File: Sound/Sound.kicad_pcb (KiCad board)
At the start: 4 copper layers, 133.6 x 74.7 mm, 35 parts, among them J1 Expansion_Connector, U1 74HCT74, U2 74HCT08, U3 74HCT21, U4 74HCT04, U5 LM386, U6 LM386, U7 LM386

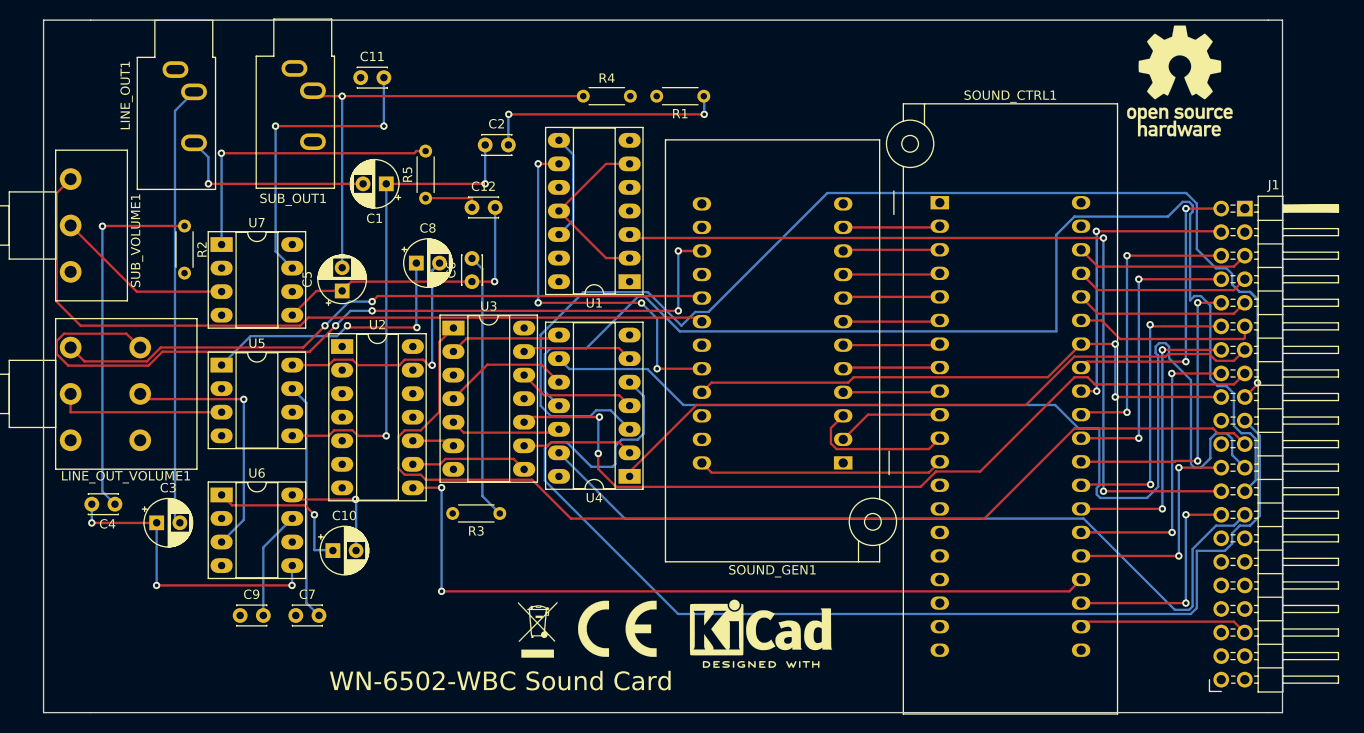
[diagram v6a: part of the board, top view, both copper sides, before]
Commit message: Fat trimming...
Trimmed out some old files and edited the docs.
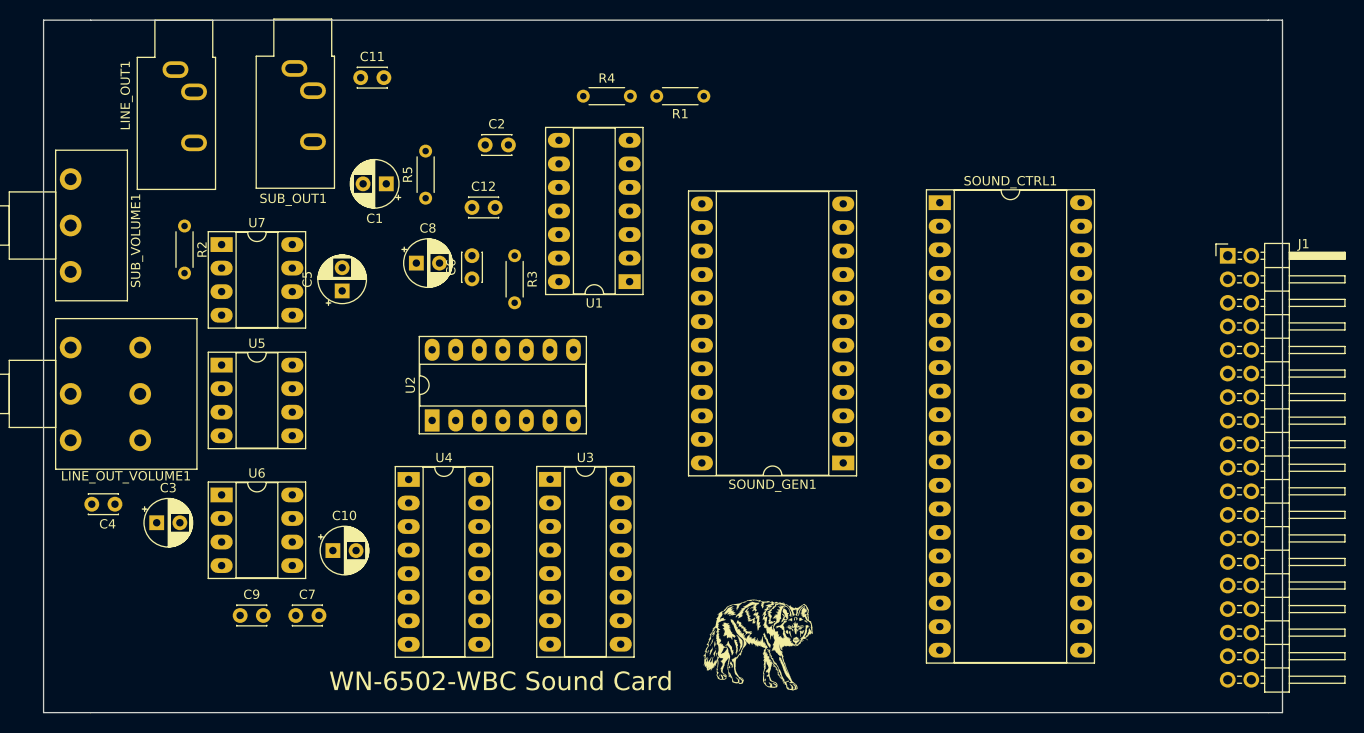
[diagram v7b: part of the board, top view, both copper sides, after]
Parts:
- removed REF**: OSHW-Logo_11.4x12mm_SilkScreen, Symbol:OSHW-Logo_11.4x12mm_SilkScreen
- removed REF**: WEEE-Logo_4.2x6mm_SilkScreen, Symbol:WEEE-Logo_4.2x6mm_SilkScreen
- removed REF**: CE-Logo_8.5x6mm_SilkScreen, Symbol:CE-Logo_8.5x6mm_SilkScreen
- removed REF**: KiCad-Logo2_6mm_SilkScreen, Symbol:KiCad-Logo2_6mm_SilkScreen
- added G***: LOGO, WolfNet:WolfNet-Logo_silkscreen, F.Cu at (128.3, 118.1)
- LINE_OUT1: value LINE OUT -> 3.5mm stereo
- SOUND_CTRL1: footprint Socket:DIP_Socket-40_W11.9_W12.7_W15.24_W17.78_W18.5_3M_240-1280-00-0602J -> Package_DIP:DIP-40_W15.24mm_Socket_LongPads
- SOUND_GEN1: footprint Socket:DIP_Socket-24_W11.9_W12.7_W15.24_W17.78_W18.5_3M_224-1275-00-0602J -> Package_DIP:DIP-24_W15.24mm_Socket_LongPads
- SUB_OUT1: value SUB OUT -> 3.5mm mono
- U2: value 74HCT08 -> 74HCT02
- U3: value 74HCT21 -> 74HCT138; footprint Package_DIP:DIP-14_W7.62mm_Socket_LongPads -> Package_DIP:DIP-16_W7.62mm_Socket_LongPads
- U4: value 74HCT04 -> 74HCT138; footprint Package_DIP:DIP-14_W7.62mm_Socket_LongPads -> Package_DIP:DIP-16_W7.62mm_Socket_LongPads
- moved R3 27.8 mm to (101.6, 76.2), turned to -90 degrees
- moved U4 23.8 mm to (90.2, 100.3), turned to 0 degrees
- moved U3 19.4 mm to (105.4, 100.3)
- moved U2 12.6 mm to (92.7, 94.0), turned to 90 degrees
- moved J1 7.14 mm to (178.5, 76.2)
- moved C6 0.30 mm to (97.0, 78.7)
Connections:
- net R\~W renamed R\~{W}
- net ~CS_SND renamed ~{CS_SND}
- net ~RESET renamed ~{RESET}
- J1 pad 20: (no net) -> unconnected-(J1-Pad20)
- J1 pad 22: (no net) -> unconnected-(J1-Pad22)
- J1 pad 28: ~CS_DEV -> CS_DEV
- J1 pad 29: (no net) -> unconnected-(J1-Pad29)
- J1 pad 30: (no net) -> unconnected-(J1-Pad30)
- J1 pad 31: (no net) -> unconnected-(J1-Pad31)
- J1 pad 32: (no net) -> unconnected-(J1-Pad32)
- J1 pad 33: (no net) -> unconnected-(J1-Pad33)
- J1 pad 34: (no net) -> unconnected-(J1-Pad34)
- J1 pad 35: (no net) -> unconnected-(J1-Pad35)
- J1 pad 36: (no net) -> unconnected-(J1-Pad36)
- J1 pad 38: (no net) -> unconnected-(J1-Pad38)
- SOUND_CTRL1 pad 13: (no net) -> unconnected-(SOUND_CTRL1-Pad13)
- SOUND_CTRL1 pad 14: (no net) -> unconnected-(SOUND_CTRL1-Pad14)
- SOUND_CTRL1 pad 15: (no net) -> unconnected-(SOUND_CTRL1-Pad15)
- SOUND_CTRL1 pad 16: (no net) -> unconnected-(SOUND_CTRL1-Pad16)
- SOUND_CTRL1 pad 17: (no net) -> unconnected-(SOUND_CTRL1-Pad17)
- SOUND_CTRL1 pad 18: (no net) -> unconnected-(SOUND_CTRL1-Pad18)
- SOUND_CTRL1 pad 19: (no net) -> unconnected-(SOUND_CTRL1-Pad19)
- SOUND_CTRL1 pad 21: (no net) -> unconnected-(SOUND_CTRL1-Pad21)
- SOUND_CTRL1 pad 23: ~CS_DEV -> Net-(SOUND_CTRL1-Pad23)
- SOUND_CTRL1 pad 24: Net-(SOUND_CTRL1-Pad24) -> CS_DEV
- SOUND_CTRL1 pad 39: (no net) -> unconnected-(SOUND_CTRL1-Pad39)
- SOUND_CTRL1 pad 40: (no net) -> unconnected-(SOUND_CTRL1-Pad40)
- SOUND_GEN1 pad 12: (no net) -> unconnected-(SOUND_GEN1-Pad12)
- SOUND_GEN1 pad 14: (no net) -> unconnected-(SOUND_GEN1-Pad14)
- SOUND_GEN1 pad 16: (no net) -> unconnected-(SOUND_GEN1-Pad16)
- U1 pad 5: (no net) -> unconnected-(U1-Pad5)
- U2 pad 1: (no net) -> Net-(SOUND_CTRL1-Pad23)
- U2 pad 10: Net-(U2-Pad10) -> (no net)
- U2 pad 2: (no net) -> Net-(U2-Pad2)
- U2 pad 3: (no net) -> Net-(U2-Pad3)
- U2 pad 8: Net-(SOUND_CTRL1-Pad24) -> (no net)
- U2 pad 9: Net-(U2-Pad9) -> (no net)
- U3 pad 1: A8 -> A4
- U3 pad 10: A5 -> unconnected-(U3-Pad10)
- U3 pad 11: (no net) -> unconnected-(U3-Pad11)
- U3 pad 12: Net-(U3-Pad12) -> unconnected-(U3-Pad12)
- U3 pad 13: Net-(U3-Pad13) -> unconnected-(U3-Pad13)
- U3 pad 14: VCC -> unconnected-(U3-Pad14)
- U3 pad 2: Net-(U3-Pad2) -> A6
- U3 pad 3: (no net) -> A7
- U3 pad 4: Net-(U3-Pad4) -> GND
- U3 pad 5: Net-(U3-Pad5) -> GND
- U3 pad 6: Net-(U2-Pad10) -> A5
- U3 pad 7: GND -> unconnected-(U3-Pad7)
- U3 pad 8: Net-(U2-Pad9) -> GND
- U3 pad 9: Net-(U3-Pad9) -> unconnected-(U3-Pad9)
- U4 pad 1: A4 -> A9
- U4 pad 10: Net-(U3-Pad4) -> unconnected-(U4-Pad10)
- U4 pad 11: A10 -> unconnected-(U4-Pad11)
- U4 pad 12: Net-(U3-Pad5) -> unconnected-(U4-Pad12)
- U4 pad 13: A11 -> unconnected-(U4-Pad13)
- U4 pad 14: VCC -> unconnected-(U4-Pad14)
- U4 pad 2: Net-(U3-Pad9) -> A10
- U4 pad 3: A6 -> A11
- U4 pad 4: Net-(U3-Pad12) -> GND
- U4 pad 5: A7 -> GND
- U4 pad 6: Net-(U3-Pad13) -> A8
- U4 pad 7: GND -> unconnected-(U4-Pad7)
- U4 pad 8: Net-(U3-Pad2) -> GND
- U4 pad 9: A9 -> unconnected-(U4-Pad9)
- U7 pad 8: (no net) -> unconnected-(U7-Pad8)
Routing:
- net GND: track 350.9 -> 0.00 mm
- net VCC: track 238.5 -> 0.00 mm
- net A10: track 129.0 -> 0.00 mm
- net A7: track 127.0 -> 0.00 mm
- net A6: track 126.0 -> 0.00 mm, vias 1 -> 0
- net A9: track 117.8 -> 0.00 mm
- net A8: track 116.8 -> 0.00 mm
- net 8MHz: track 91.3 -> 0.00 mm, vias 2 -> 0
- net Net-(LINE_OUT_VOLUME1-Pad4): track 90.3 -> 0.00 mm, vias 4 -> 0
- net A5: track 90.2 -> 0.00 mm, vias 2 -> 0
- net A11: track 88.8 -> 0.00 mm
- net Net-(SOUND_GEN1-Pad18): track 85.0 -> 0.00 mm
- net Net-(SOUND_CTRL1-Pad24): track 83.8 -> 0.00 mm, vias 2 -> 0
- net A4: track 72.9 -> 0.00 mm
- net Net-(LINE_OUT_VOLUME1-Pad1): track 71.7 -> 0.00 mm, vias 2 -> 0
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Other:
- net class Default removed

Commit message: 406 traces left to route...
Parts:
- moved G*** 48.3 mm to (176.5, 118.1)
- moved U2 39.5 mm to (125.7, 115.6), turned to 180 degrees
- moved J1 21.6 mm to (177.2, 54.6)
- moved SOUND_GEN1 16.1 mm to (138.4, 82.6)
- moved SOUND_CTRL1 15.9 mm to (147.4, 54.6)
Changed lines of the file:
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@@
   )
   (footprint "PC:Expansion_Connector_Board" (layer "F.Cu")
-    (at 178.5 76.21)
+    (at 177.23 54.62)
     (descr "Through hole angled pin header, 2x19, 2.54mm pitch, 6mm pin length, double rows")
     (tags "Through hole angled pin header THT 2x19 2.54mm double row")
@@
   )
   (footprint "Package_DIP:DIP-24_W15.24mm_Socket_LongPads" (layer "F.Cu")
-    (at 137.033 98.552 180)
+    (at 138.435 82.555 180)
     (descr "24-lead though-hole mounted DIP package, row spacing 15.24 mm (600 mils), Socket, LongPads")
     (tags "THT DIP DIL PDIP 2.54mm 15.24mm 600mil Socket LongPads")
@@
   )
   (footprint "Package_DIP:DIP-40_W15.24mm_Socket_LongPads" (layer "F.Cu")
-    (at 147.447 70.485)
+    (at 147.447 54.615)
     (descr "40-lead though-hole mounted DIP package, row spacing 15.24 mm (600 mils), Socket, LongPads")
     (tags "THT DIP DIL PDIP 2.54mm 15.24mm 600mil Socket LongPads")
@@
   )
   (footprint "WolfNet:WolfNet-Logo_silkscreen" (layer "F.Cu")
-    (at 128.27 118.11)
+    (at 176.53 118.11)
     (attr through_hole)
     (fp_text reference "G***" (at 0 0) (layer "F.SilkS") hide
@@
   )
   (footprint "Package_DIP:DIP-14_W7.62mm_Socket_LongPads" (layer "F.Cu")
-    (at 92.705 93.97 90)
+    (at 125.72 115.575 180)
     (descr "14-lead though-hole mounted DIP package, row spacing 7.62 mm (300 mils), Socket, LongPads")
     (tags "THT DIP DIL PDIP 2.54mm 7.62mm 300mil Socket LongPads")
@@
     (property "Sheetname" "")
     (attr through_hole)
-    (fp_text reference "U2" (at 3.81 -2.33 90) (layer "F.SilkS")
+    (fp_text reference "U2" (at 3.81 -2.33) (layer "F.SilkS")
       (effects (font (size 1 1) (thickness 0.15)))
     )
-    (fp_text value "74HCT02" (at 3.81 17.57 90) (layer "F.Fab")
+    (fp_text value "74HCT02" (at 3.81 17.57) (layer "F.Fab")
       (effects (font (size 1 1) (thickness 0.15)))
     )
-    (fp_text user "${REFERENCE}" (at 3.81 7.62 90) (layer "F.Fab")
+    (fp_text user "${REFERENCE}" (at 3.81 7.62) (layer "F.Fab")
       (effects (font (size 1 1) (thickness 0.15)))
     )
@@
     (fp_line (start -1.27 16.57) (end 8.89 16.57) (layer "F.Fab") (width 0.1))
     (fp_line (start -1.27 -1.33) (end -1.27 16.57) (layer "F.Fab") (width 0.1))
-    (pad "1" thru_hole rect (at 0 0 90) (size 2.4 1.6) (drill 0.8) (layers *.Cu *.Mask)
+    (pad "1" thru_hole rect (at 0 0 180) (size 2.4 1.6) (drill 0.8) (layers *.Cu *.Mask)
       (net 78 "Net-(SOUND_CTRL1-Pad23)") (pintype "output"))
-    (pad "2" thru_hole oval (at 0 2.54 90) (size 2.4 1.6) (drill 0.8) (layers *.Cu *.Mask)
+    (pad "2" thru_hole oval (at 0 2.54 180) (size 2.4 1.6) (drill 0.8) (layers *.Cu *.Mask)
       (net 93 "Net-(U2-Pad2)") (pintype "input"))
-    (pad "3" thru_hole oval (at 0 5.08 90) (size 2.4 1.6) (drill 0.8) (layers *.Cu *.Mask)
+    (pad "3" thru_hole oval (at 0 5.08 180) (size 2.4 1.6) (drill 0.8) (layers *.Cu *.Mask)
       (net 94 "Net-(U2-Pad3)") (pintype "input"))
-    (pad "4" thru_hole oval (at 0 7.62 90) (size 2.4 1.6) (drill 0.8) (layers *.Cu *.Mask))
-    (pad "5" thru_hole oval (at 0 10.16 90) (size 2.4 1.6) (drill 0.8) (layers *.Cu *.Mask))
-    (pad "6" thru_hole oval (at 0 12.7 90) (size 2.4 1.6) (drill 0.8) (layers *.Cu *.Mask))
-    (pad "7" thru_hole oval (at 0 15.24 90) (size 2.4 1.6) (drill 0.8) (layers *.Cu *.Mask)
+    (pad "4" thru_hole oval (at 0 7.62 180) (size 2.4 1.6) (drill 0.8) (layers *.Cu *.Mask))
+    (pad "5" thru_hole oval (at 0 10.16 180) (size 2.4 1.6) (drill 0.8) (layers *.Cu *.Mask))
+    (pad "6" thru_hole oval (at 0 12.7 180) (size 2.4 1.6) (drill 0.8) (layers *.Cu *.Mask))
+    (pad "7" thru_hole oval (at 0 15.24 180) (size 2.4 1.6) (drill 0.8) (layers *.Cu *.Mask)
       (net 2 "GND") (pinfunction "GND") (pintype "power_in"))
-    (pad "8" thru_hole oval (at 7.62 15.24 90) (size 2.4 1.6) (drill 0.8) (layers *.Cu *.Mask))
-    (pad "9" thru_hole oval (at 7.62 12.7 90) (size 2.4 1.6) (drill 0.8) (layers *.Cu *.Mask))
-    (pad "10" thru_hole oval (at 7.62 10.16 90) (size 2.4 1.6) (drill 0.8) (layers *.Cu *.Mask))
-    (pad "11" thru_hole oval (at 7.62 7.62 90) (size 2.4 1.6) (drill 0.8) (layers *.Cu *.Mask))
-    (pad "12" thru_hole oval (at 7.62 5.08 90) (size 2.4 1.6) (drill 0.8) (layers *.Cu *.Mask))
-    (pad "13" thru_hole oval (at 7.62 2.54 90) (size 2.4 1.6) (drill 0.8) (layers *.Cu *.Mask))
-    (pad "14" thru_hole oval (at 7.62 0 90) (size 2.4 1.6) (drill 0.8) (layers *.Cu *.Mask)
+    (pad "8" thru_hole oval (at 7.62 15.24 180) (size 2.4 1.6) (drill 0.8) (layers *.Cu *.Mask))
+    (pad "9" thru_hole oval (at 7.62 12.7 180) (size 2.4 1.6) (drill 0.8) (layers *.Cu *.Mask))
+    (pad "10" thru_hole oval (at 7.62 10.16 180) (size 2.4 1.6) (drill 0.8) (layers *.Cu *.Mask))
+    (pad "11" thru_hole oval (at 7.62 7.62 180) (size 2.4 1.6) (drill 0.8) (layers *.Cu *.Mask))
+    (pad "12" thru_hole oval (at 7.62 5.08 180) (size 2.4 1.6) (drill 0.8) (layers *.Cu *.Mask))
+    (pad "13" thru_hole oval (at 7.62 2.54 180) (size 2.4 1.6) (drill 0.8) (layers *.Cu *.Mask))
+    (pad "14" thru_hole oval (at 7.62 0 180) (size 2.4 1.6) (drill 0.8) (layers *.Cu *.Mask)
       (net 27 "VCC") (pinfunction "VCC") (pintype "power_in"))
     (model "${KICAD6_3DMODEL_DIR}/Package_DIP.3dshapes/DIP-14_W7.62mm_Socket.wrl"
@@
   )
   (dimension (type aligned) (layer "Dwgs.User")
-    (pts (xy 193.04 50.8) (xy 193.04 125.476))
-    (height 0)
-    (gr_text "74.6760 mm" (at 191.89 88.138 90) (layer "Dwgs.User")
-      (effects (font (size 1 1) (thickness 0.15)))
+    (pts (xy 184.15 125.476) (xy 184.15 54.61))
+    (height 10.16)
+    (gr_text "70.8660 mm" (at 192.51 90.043 90) (layer "Dwgs.User")
+      (effects (font (size 1.5 1.5) (thickness 0.3)))
     )
-    (format (units 2) (units_format 1) (precision 4))
-    (style (thickness 0.15) (arrow_length 1.27) (text_position_mode 0) (extension_height 0.58642) (extension_offset 0) keep_text_aligned)
+    (format (units 3) (units_format 1) (precision 4))
+    (style (thickness 0.2) (arrow_length 1.27) (text_position_mode 0) (extension_height 0.58642) (extension_offset 0.5) keep_text_aligned)
   )
   (dimension (type aligned) (layer "Dwgs.User")
